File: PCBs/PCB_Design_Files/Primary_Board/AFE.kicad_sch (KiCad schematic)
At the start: 25 parts, among them U1 OPA381, U2 TLV9002, U4 TLV9002

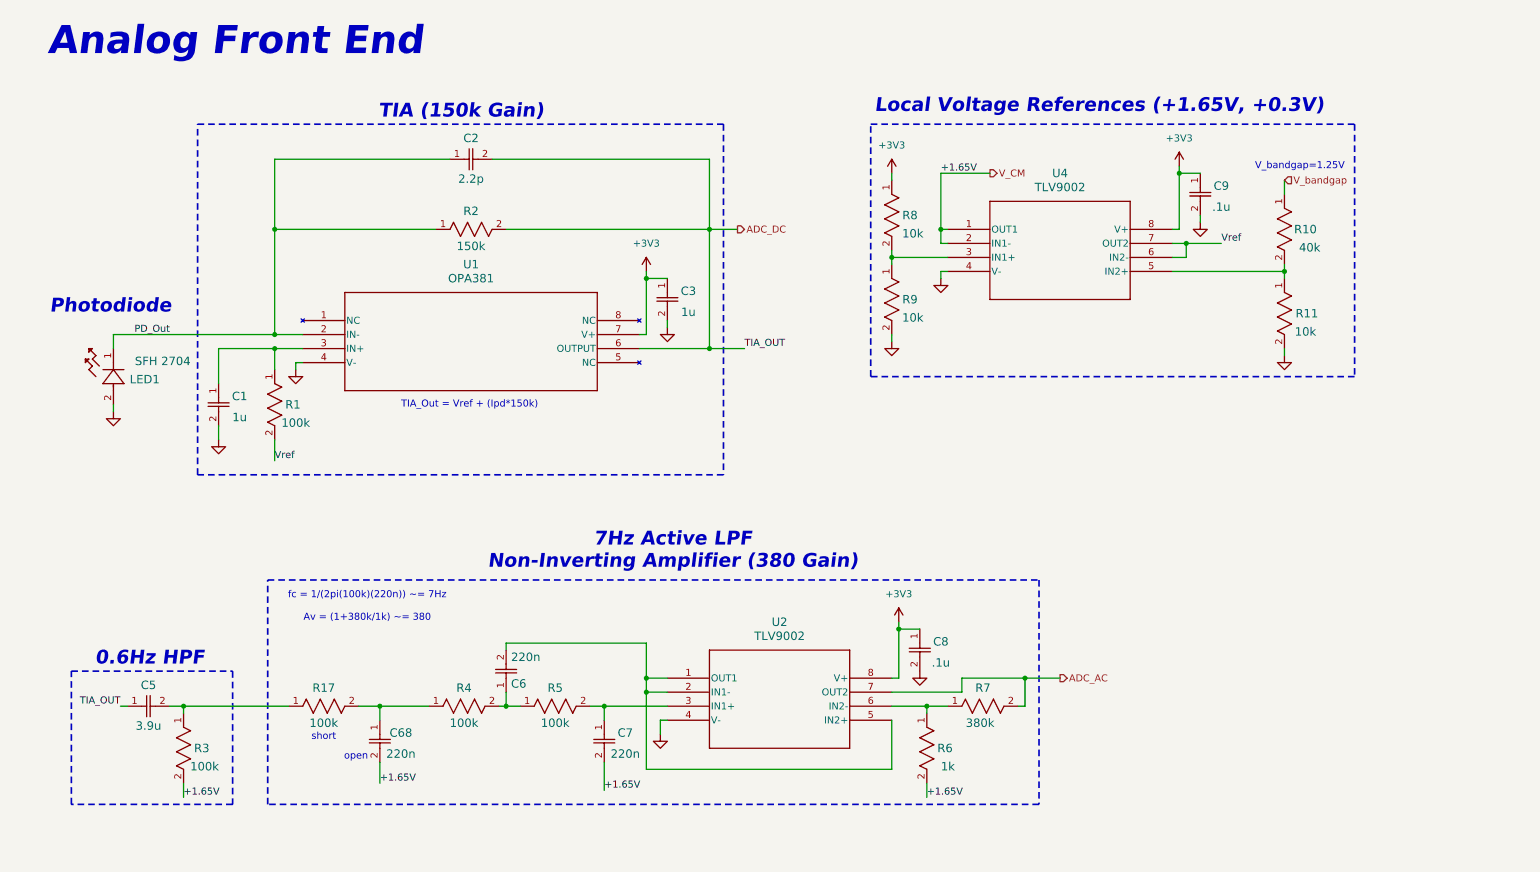
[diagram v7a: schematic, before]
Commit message: updated soldered values
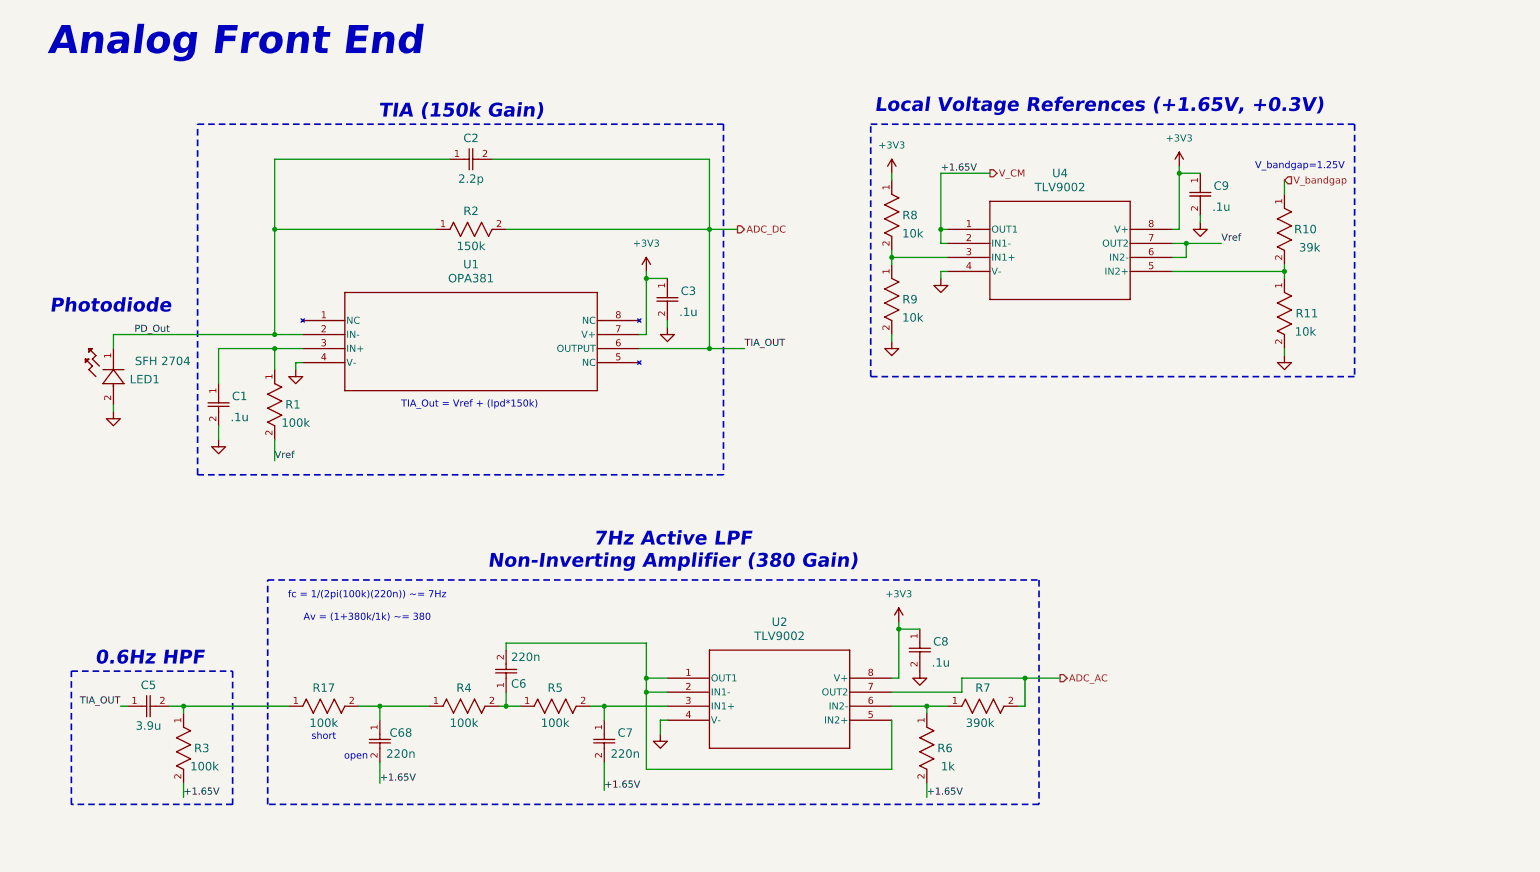
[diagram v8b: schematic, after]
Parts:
- C1, C3: value 1u -> .1u
- R10: value 40k -> 39k
- R7: value 380k -> 390k
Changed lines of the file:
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@@
 			)
 		)
-		(property "Value" "1u"
+		(property "Value" ".1u"
 			(at 129.54 68.326 90)
 			(effects
@@
 			)
 		)
-		(property "Value" "40k"
+		(property "Value" "39k"
 			(at 242.062 56.642 90)
 			(effects
@@
 			)
 		)
-		(property "Value" "1u"
+		(property "Value" ".1u"
 			(at 48.26 87.376 90)
 			(effects
@@
 			)
 		)
-		(property "Value" "380k"
+		(property "Value" "390k"
 			(at 182.372 142.748 0)
 			(effects
